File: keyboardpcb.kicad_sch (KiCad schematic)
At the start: 13 parts, among them SW1 SW_Push, U1 ATmega32U4-A, Y1 16MHz

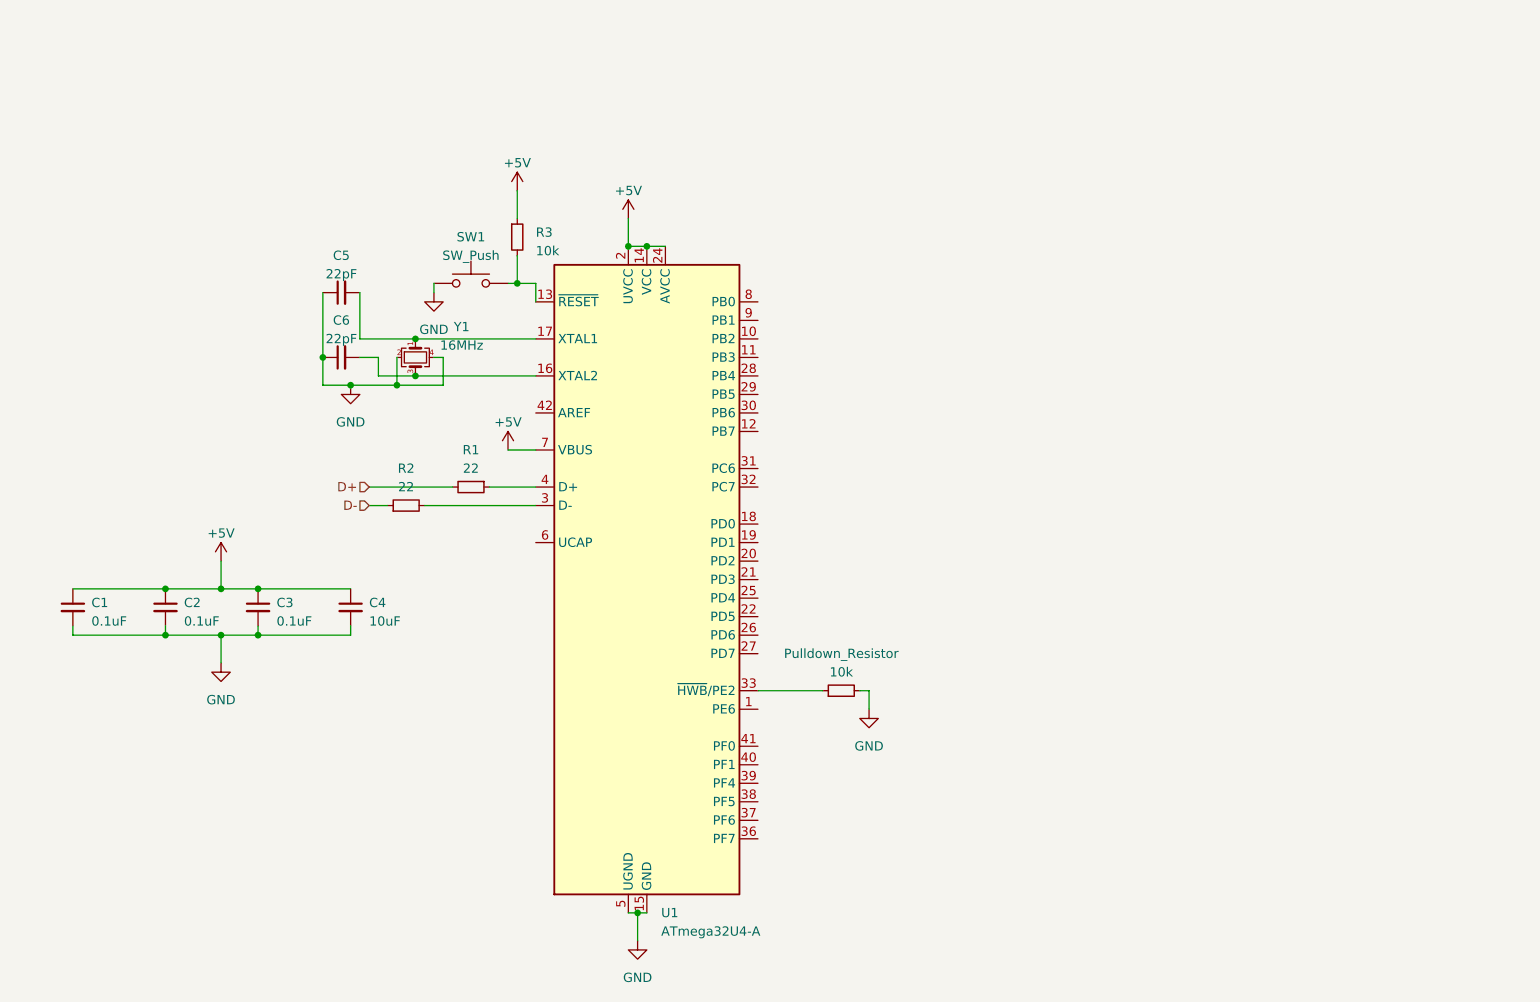
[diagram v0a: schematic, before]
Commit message: Finished the schematic
2x2 keyboard schematic for testing
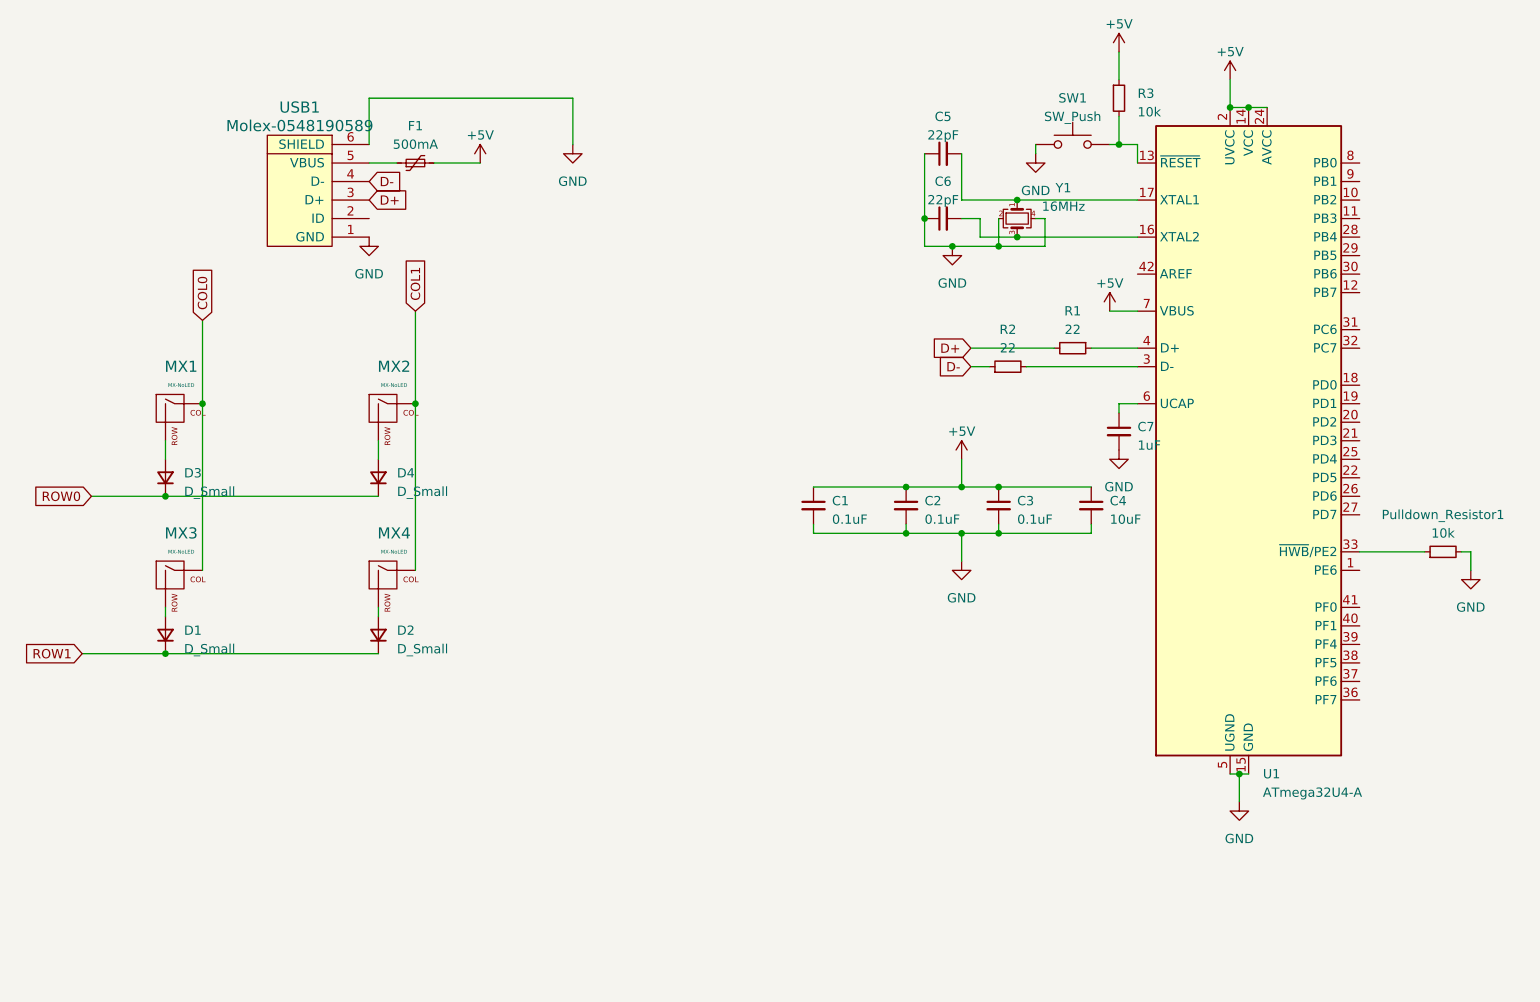
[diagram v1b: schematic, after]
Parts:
- added C7: 1uF, Capacitor_SMD:C_0805_2012Metric, symbol Device:C_Small
- added D1, D2, D3, D4: D_Small, Diode_SMD:D_SOD-123, symbol Device:D_Small
- added F1: 500mA, Fuse:Fuse_1206_3216Metric, symbol Device:Polyfuse_Small
- added MX1, MX2, MX3, MX4: MX-NoLED, MX_Alps_Hybrid:MX-1U, symbol MX_Alps_Hybrid:MX-NoLED
- added USB1: Molex-0548190589, random-keyboard-parts:Molex-0548190589, symbol random-keyboard-parts:Molex-0548190589
- C1, C2, C3, C4, C5, C6: footprint (none) -> Capacitor_SMD:C_0805_2012Metric
- Pulldown_Resistor1: renamed from Pulldown_Resistor; footprint (none) -> Resistor_SMD:R_0805_2012Metric
- R1, R2, R3: footprint (none) -> Resistor_SMD:R_0805_2012Metric
- SW1: footprint (none) -> random-keyboard-parts:SKQG-1155865
- Y1: footprint (none) -> Crystal:Crystal_SMD_3225-4Pin_3.2x2.5mm
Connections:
- net +5V: now also F1.2
- net D+: now also USB1.3 (D+)
- net D-: now also USB1.4 (D-)
- net GND: now also C7.2, USB1.1 (GND), USB1.6 (SHIELD)
- net at U1.6 (UCAP): now also C7.1
- new net: D2.2 (A), MX4.2 (ROW)
- new net: D4.2 (A), MX2.2 (ROW)
- new net: F1.1, USB1.5 (VBUS)
- new net: D3.2 (A), MX1.2 (ROW)
- new net: D1.2 (A), MX3.2 (ROW)
- new net COL0: MX1.1 (COL), MX3.1 (COL)
- new net COL1: MX2.1 (COL), MX4.1 (COL)
- new net ROW0: D3.1 (K), D4.1 (K)
- new net ROW1: D1.1 (K), D2.1 (K)
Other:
- moved on the sheet: C1, C2, C3, C4, C5, C6, Pulldown_Resistor1, R1, R2, R3, SW1, U1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
